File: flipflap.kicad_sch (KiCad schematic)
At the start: 27 parts, among them J1 Conn_01x03, J2 Conn_01x02, U1 TPIC6C595DR, U2 TPIC6C595DR, U3 TPIC6C595DR, U4 74LV165AD, U5 D1 mini, X1 WSL20G, X10 Conn_01x03, X2 WSL20G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

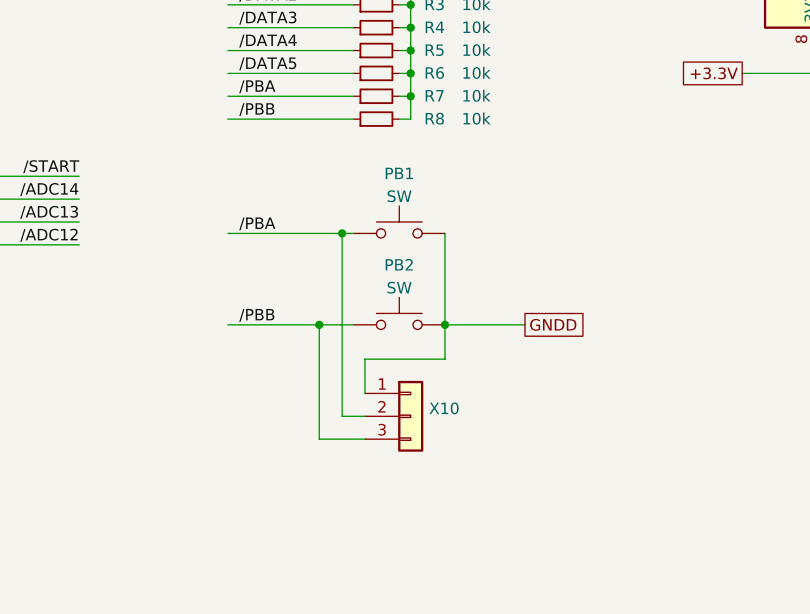
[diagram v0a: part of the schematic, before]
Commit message: Add footprints to all parts
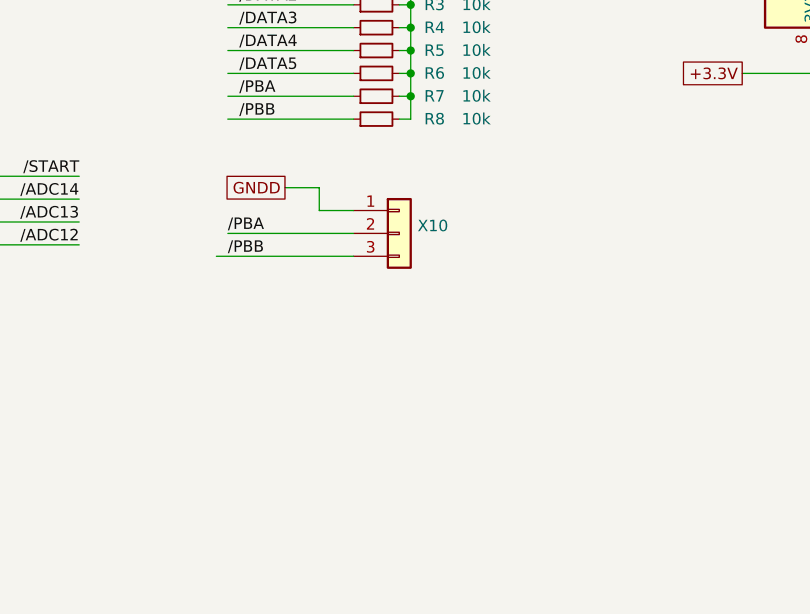
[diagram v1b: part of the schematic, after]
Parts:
- removed PB1, PB2: SW, symbol Switch:SW_Push
- J1: footprint (none) -> Connector_PinHeader_2.54mm:PinHeader_1x02_P2.54mm_Vertical
- J2, X10: footprint (none) -> Connector_PinHeader_2.54mm:PinHeader_1x03_P2.54mm_Vertical
- R1, R2, R3, R4, R5, R6, R7, R8: footprint (none) -> Resistor_SMD:R_0603_1608Metric
- U1, U2, U3, U4: footprint (none) -> Package_SO:SOIC-16_3.9x9.9mm_P1.27mm
- X1, X2, X3, X4, X5, X6, X7, X8: footprint (none) -> Connector_PinHeader_2.54mm:PinHeader_2x10_P2.54mm_Vertical
- X9: footprint (none) -> Connector_PinHeader_2.54mm:PinHeader_2x08_P2.54mm_Vertical
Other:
- moved on the sheet: X10

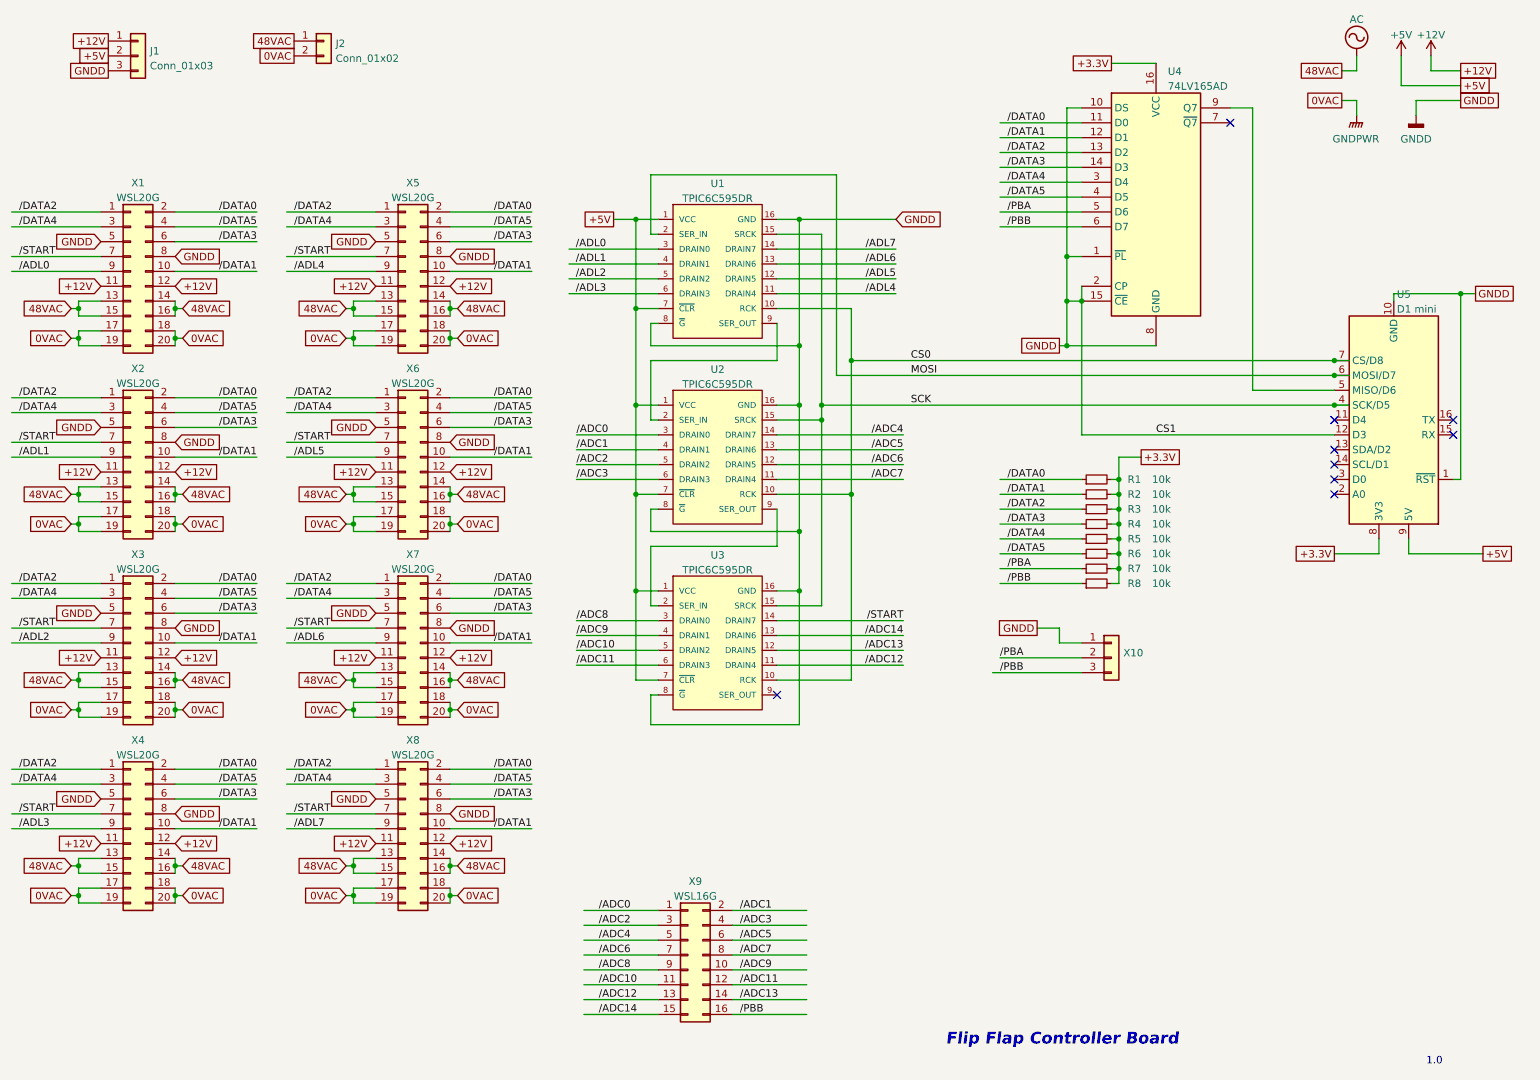
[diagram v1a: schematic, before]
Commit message: Completed PCB, populated on both sides.
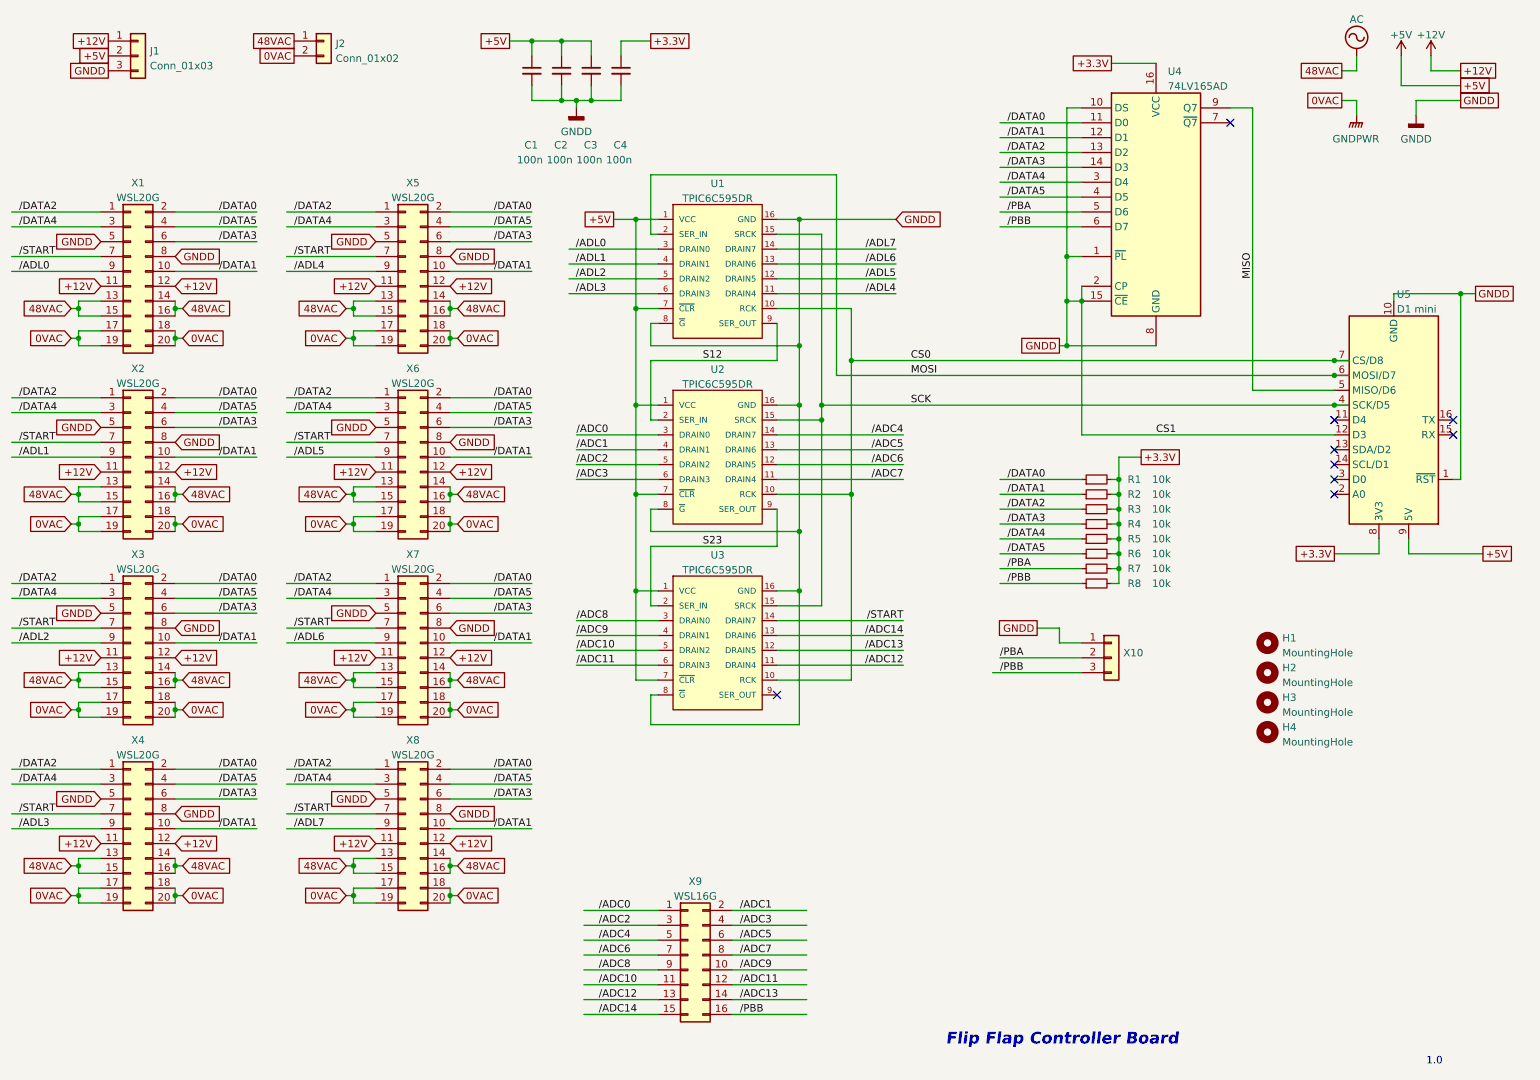
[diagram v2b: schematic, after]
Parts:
- added C1, C2, C3, C4: 100n, Capacitor_SMD:C_0603_1608Metric, symbol Device:C_Small
- added H1, H2, H3, H4: MountingHole, MountingHole:MountingHole_3.5mm, symbol Mechanical:MountingHole
- J1: footprint Connector_PinHeader_2.54mm:PinHeader_1x02_P2.54mm_Vertical -> Connector_PinHeader_2.54mm:PinHeader_1x03_P2.54mm_Vertical
- J2: footprint Connector_PinHeader_2.54mm:PinHeader_1x03_P2.54mm_Vertical -> Connector_PinHeader_2.54mm:PinHeader_1x02_P2.54mm_Vertical
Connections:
- net +3.3V: now also C4.1
- net +5V: now also C1.1, C2.1, C3.1
- net GNDD: now also C1.2, C2.2, C3.2, C4.2
- net MISO: now reaches U4.9 (Q7), U5.5 (MISO/D6)
- net S12: now reaches U1.9 (SER_OUT), U2.2 (SER_IN)
- net S23: now reaches U2.9 (SER_OUT), U3.2 (SER_IN)

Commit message: Complete PCB with components only on one side, some corrections included
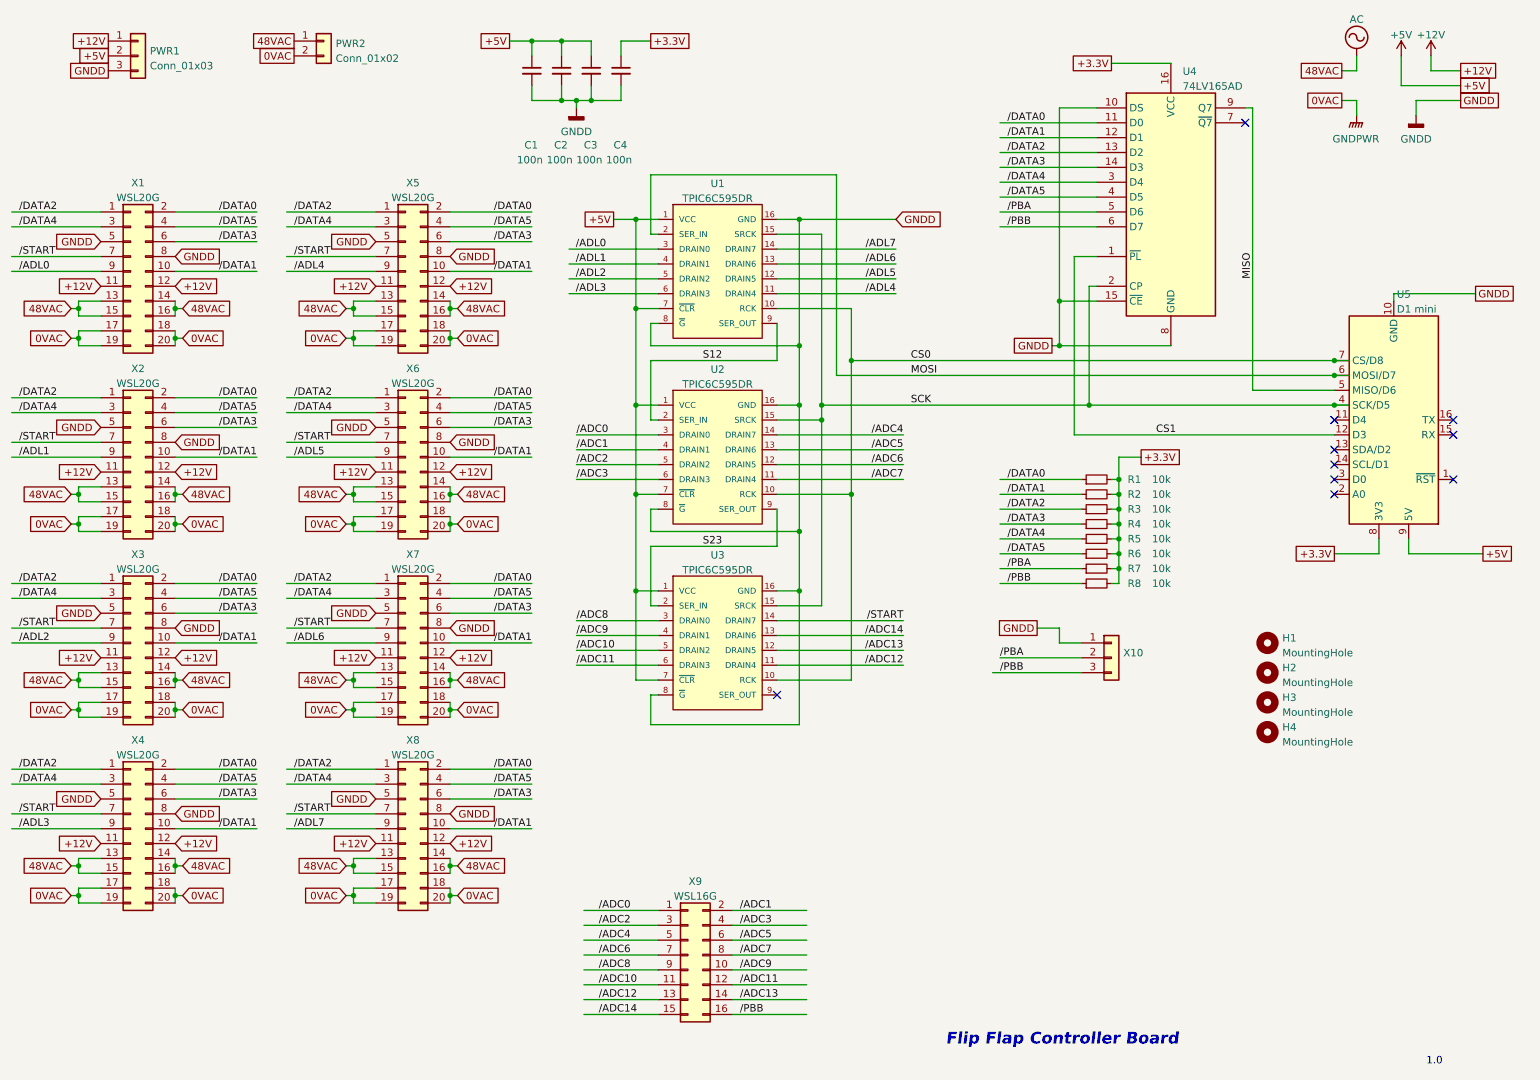
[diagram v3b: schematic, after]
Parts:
- X1, X2, X3, X4, X5, X6, X7, X8: footprint Connector_PinHeader_2.54mm:PinHeader_2x10_P2.54mm_Vertical -> Connector_IDC:IDC-Header_2x10_P2.54mm_Vertical
- X9: footprint Connector_PinHeader_2.54mm:PinHeader_2x08_P2.54mm_Vertical -> Connector_IDC:IDC-Header_2x08_P2.54mm_Vertical
- renumbered J1 to PWR1, J2 to PWR2
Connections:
- net GNDD: no longer U4.1 (~{PL}), U4.2 (CP), U5.1 (~{RST}), U5.12 (D3)
- net SCK: now also U4.2 (CP)
- new net CS1: U4.1 (~{PL}), U5.12 (D3)
- no-connect marks 9 -> 10
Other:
- moved on the sheet: U4

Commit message: As ordered from JLCPCB
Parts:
- C1, C2, C4: JLCPCB (none) -> C14663
- R1, R2, R3, R4, R5, R6, R7, R8: JLCPCB (none) -> C4184
- U1, U2, U3: JLCPCB (none) -> C350572
- U4: JLCPCB (none) -> C478150
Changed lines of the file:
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@@
+      (effects (font (size 1.27 1.27)) hide)
+    )
+    (property "JLCPCB" "C4184" (id 4) (at 212.09 96.52 90)
       (effects (font (size 1.27 1.27)) hide)
     )
@@
       (effects (font (size 1.27 1.27)) hide)
     )
+    (property "JLCPCB" "C14663" (id 4) (at 120.65 24.13 0)
+      (effects (font (size 1.27 1.27)) hide)
+    )
     (pin "1")
     (pin "2")
@@
     )
     (property "Datasheet" "https://assets.nexperia.com/documents/data-sheet/74HC_HCT165.pdf" (id 3) (at 224.79 45.72 0)
+      (effects (font (size 1.27 1.27)) hide)
+    )
+    (property "JLCPCB" "C478150" (id 4) (at 224.79 45.72 0)
       (effects (font (size 1.27 1.27)) hide)
     )
@@
     )
     (property "Datasheet" "~" (id 3) (at 212.09 106.68 0)
+      (effects (font (size 1.27 1.27)) hide)
+    )
+    (property "JLCPCB" "C4184" (id 4) (at 212.09 106.68 90)
       (effects (font (size 1.27 1.27)) hide)
     )
@@
       (effects (font (size 1.524 1.524)))
     )
+    (property "JLCPCB" "C350572" (id 4) (at 147.32 90.17 0)
+      (effects (font (size 1.27 1.27)) hide)
+    )
     (pin "1")
     (pin "10")
@@
     )
     (property "Datasheet" "~" (id 3) (at 212.09 111.76 0)
+      (effects (font (size 1.27 1.27)) hide)
+    )
+    (property "JLCPCB" "C4184" (id 4) (at 212.09 111.76 90)
       (effects (font (size 1.27 1.27)) hide)
     )
@@
       (effects (font (size 1.524 1.524)))
     )
+    (property "JLCPCB" "C350572" (id 4) (at 147.32 121.92 0)
+      (effects (font (size 1.27 1.27)) hide)
+    )
     (pin "1")
     (pin "10")
@@
     )
     (property "Datasheet" "~" (id 3) (at 125.73 24.13 0)
+      (effects (font (size 1.27 1.27)) hide)
+    )
+    (property "JLCPCB" "" (id 4) (at 125.73 24.13 0)
       (effects (font (size 1.27 1.27)) hide)
     )
@@
       (effects (font (size 1.27 1.27)) hide)
     )
+    (property "JLCPCB" "C4184" (id 4) (at 212.09 104.14 90)
+      (effects (font (size 1.27 1.27)) hide)
+    )
     (pin "1")
     (pin "2")
@@
       (effects (font (size 1.27 1.27)) hide)
     )
+    (property "JLCPCB" "C4184" (id 4) (at 212.09 109.22 90)
+      (effects (font (size 1.27 1.27)) hide)
+    )
     (pin "1")
     (pin "2")
@@
     )
     (property "Datasheet" "~" (id 3) (at 212.09 99.06 0)
+      (effects (font (size 1.27 1.27)) hide)
+    )
+    (property "JLCPCB" "C4184" (id 4) (at 212.09 99.06 90)
       (effects (font (size 1.27 1.27)) hide)
     )
@@
     )
     (property "Datasheet" "~" (id 3) (at 212.09 101.6 0)
+      (effects (font (size 1.27 1.27)) hide)
+    )
+    (property "JLCPCB" "C4184" (id 4) (at 212.09 101.6 90)
       (effects (font (size 1.27 1.27)) hide)
     )
@@
       (effects (font (size 1.524 1.524)))
     )
+    (property "JLCPCB" "C350572" (id 4) (at 147.32 58.42 0)
+      (effects (font (size 1.27 1.27)) hide)
+    )
     (pin "1")
     (pin "10")
@@
     )
     (property "Datasheet" "~" (id 3) (at 115.57 24.13 0)
+      (effects (font (size 1.27 1.27)) hide)
+    )
+    (property "JLCPCB" "C14663" (id 4) (at 115.57 24.13 0)
       (effects (font (size 1.27 1.27)) hide)
     )
@@
       (effects (font (size 1.27 1.27)) hide)
     )
+    (property "JLCPCB" "C4184" (id 4) (at 212.09 93.98 90)
+      (effects (font (size 1.27 1.27)) hide)
+    )
     (pin "1")
     (pin "2")
@@
       (effects (font (size 1.27 1.27)) hide)
     )
+    (property "JLCPCB" "C14663" (id 4) (at 130.81 24.13 0)
+      (effects (font (size 1.27 1.27)) hide)
+    )

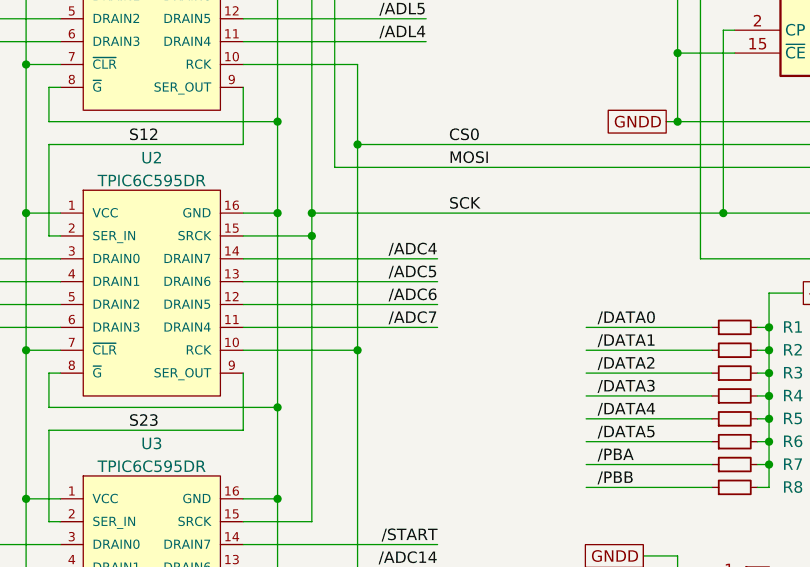
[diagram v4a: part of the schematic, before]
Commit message: Fix ADC4 to ADC7 (were swapped)
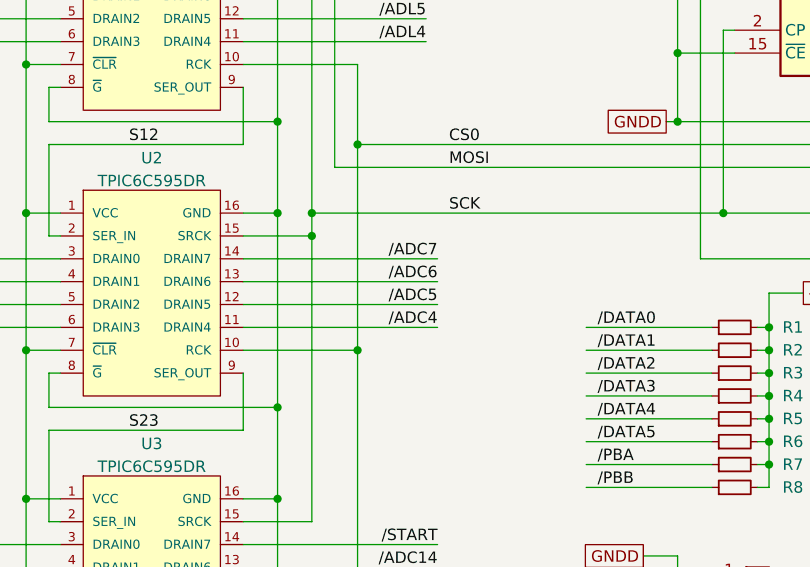
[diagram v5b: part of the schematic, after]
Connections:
- net /ADC4: now also U2.11 (DRAIN4); no longer U2.14 (DRAIN7)
- net /ADC5: now also U2.12 (DRAIN5); no longer U2.13 (DRAIN6)
- net /ADC6: now also U2.13 (DRAIN6); no longer U2.12 (DRAIN5)
- net /ADC7: now also U2.14 (DRAIN7); no longer U2.11 (DRAIN4)
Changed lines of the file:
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@@
     (effects (font (size 1.27 1.27)) (justify left bottom))
   )
-  (label "{slash}ADC7" (at 179.07 93.98 180)
+  (label "{slash}ADC4" (at 179.07 93.98 180)
     (effects (font (size 1.27 1.27)) (justify right bottom))
   )
@@
     (effects (font (size 1.27 1.27)) (justify left bottom))
   )
-  (label "{slash}ADC4" (at 179.07 86.36 180)
+  (label "{slash}ADC7" (at 179.07 86.36 180)
     (effects (font (size 1.27 1.27)) (justify right bottom))
   )
@@
     (effects (font (size 1.27 1.27)) (justify right bottom))
   )
-  (label "{slash}ADC6" (at 179.07 91.44 180)
+  (label "{slash}ADC5" (at 179.07 91.44 180)
     (effects (font (size 1.27 1.27)) (justify right bottom))
   )
@@
     (effects (font (size 1.27 1.27)) (justify right bottom))
   )
-  (label "{slash}ADC5" (at 179.07 88.9 180)
-    (effects (font (size 1.27 1.27)) (justify right bottom))
-  )
+  (label "{slash}ADC6" (at 179.07 88.9 180)
+    (effects (font (size 1.27 1.27)) (justify right bottom))
+  )
